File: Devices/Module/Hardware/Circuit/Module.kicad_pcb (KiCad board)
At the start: 2 copper layers, 7 parts, among them J1 Screw_Terminal_01x03, J2 Screw_Terminal_01x04, J3 Screw_Terminal_01x02, Q1 Q_NPN_BCE, Q2 Q_NPN_BCE

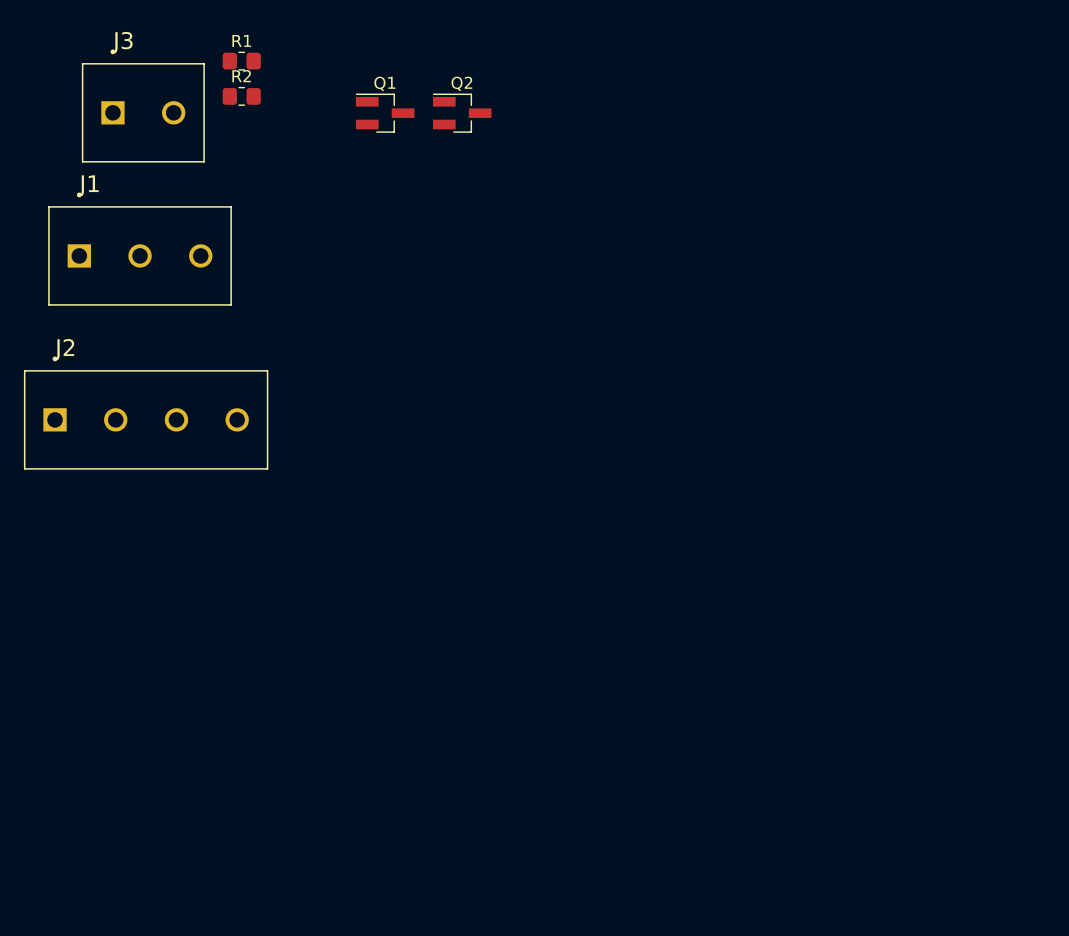
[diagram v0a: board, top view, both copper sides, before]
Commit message: Finish module PCB layout
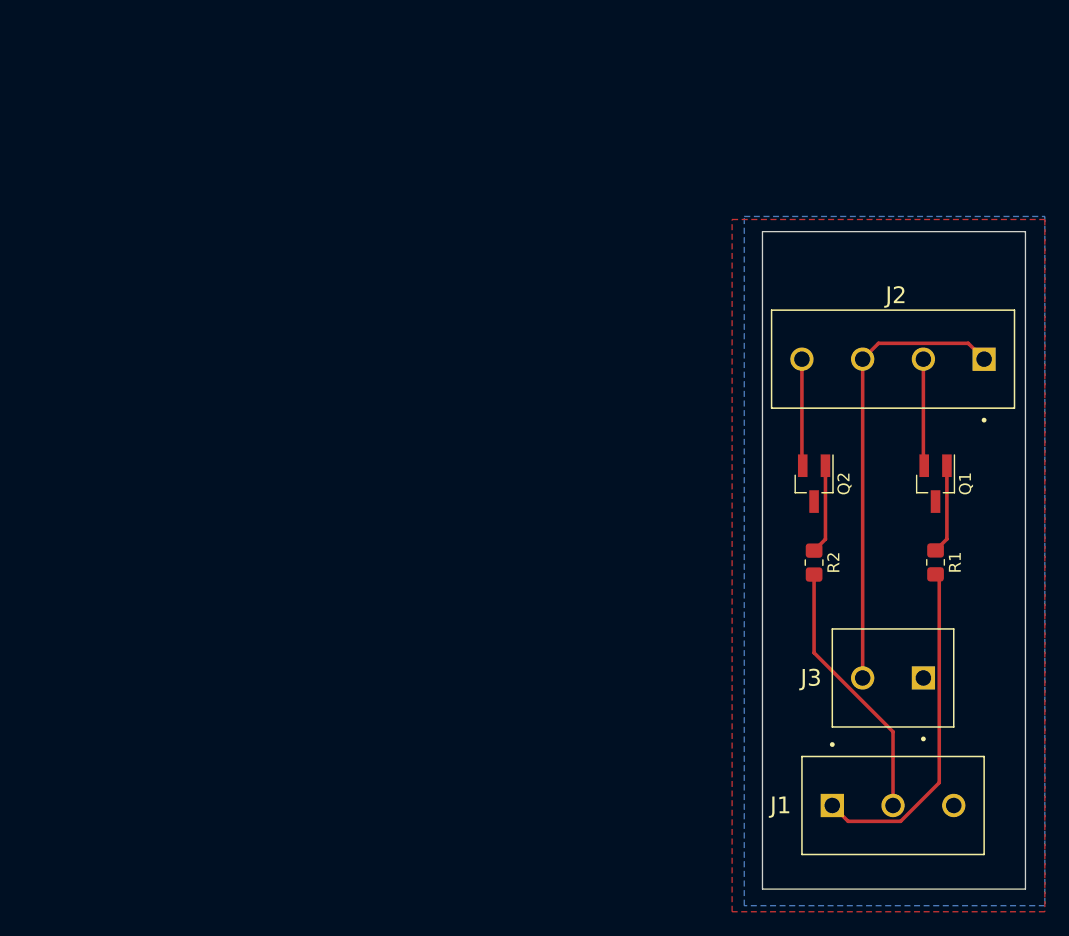
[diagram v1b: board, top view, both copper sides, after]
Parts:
- moved J3 82.7 mm to (150.1, 84.1), turned to 180 degrees
- moved J1 78.0 mm to (142.5, 94.7)
- moved J2 77.9 mm to (155.2, 57.4), turned to 180 degrees
- moved R1 71.6 mm to (151.1, 74.4), turned to 270 degrees
- moved R2 61.8 mm to (141.0, 74.4), turned to 270 degrees
- moved Q1 55.5 mm to (151.1, 67.8), turned to 270 degrees
- moved Q2 42.7 mm to (141.0, 67.8), turned to 270 degrees
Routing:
- net VCC: track 0.00 -> 37.9 mm
- net SIG1: track 0.00 -> 28.4 mm
- net SIG2: track 0.00 -> 22.1 mm
- net LED2N: track 0.00 -> 8.94 mm
- net LED1N: track 0.00 -> 8.94 mm
- net Net-(Q2-Pad1): track 0.00 -> 7.50 mm
- net Net-(Q1-Pad1): track 0.00 -> 7.48 mm
- added copper zone on B.Cu, net GND
- added copper zone on F.Cu, net GND
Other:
- board outline added: 22 x 55 mm
- board text added: "GHOSCHT - 2021"
- board text added: "v01"

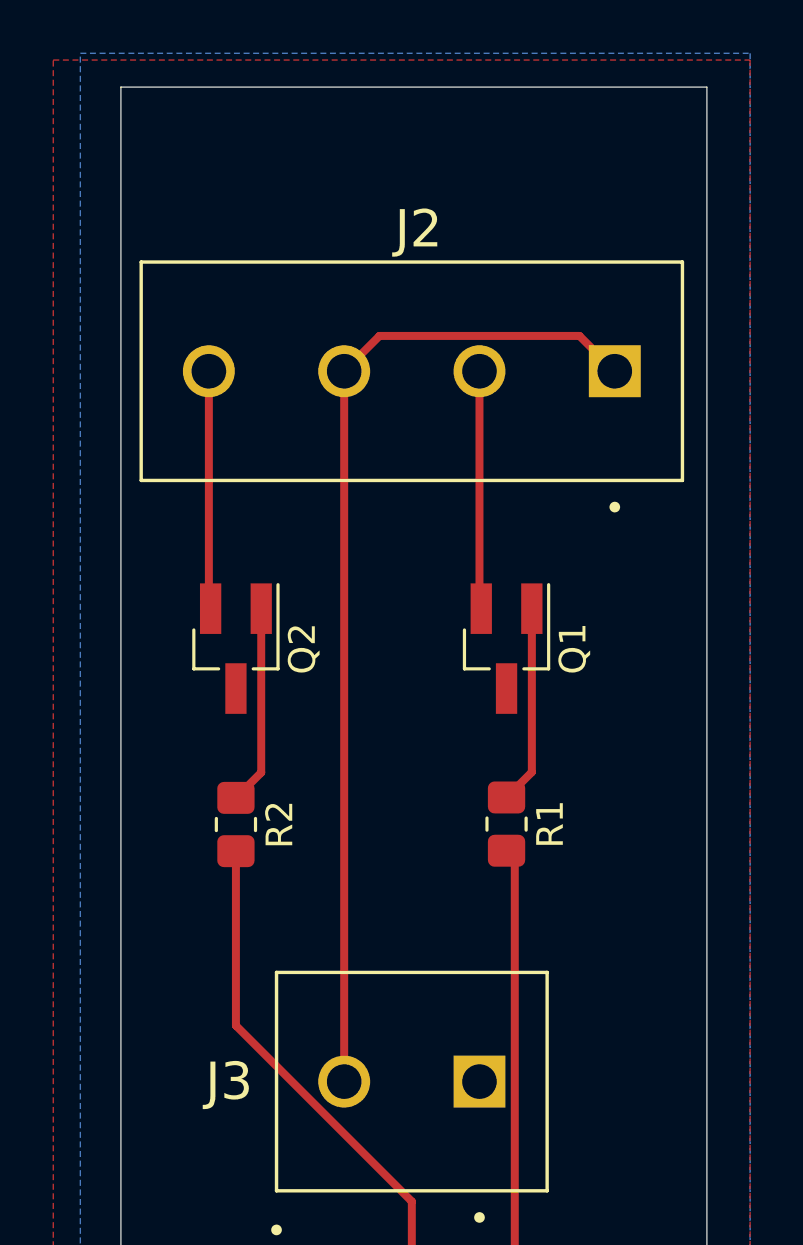
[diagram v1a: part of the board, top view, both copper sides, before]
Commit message: Add pulldown resistor
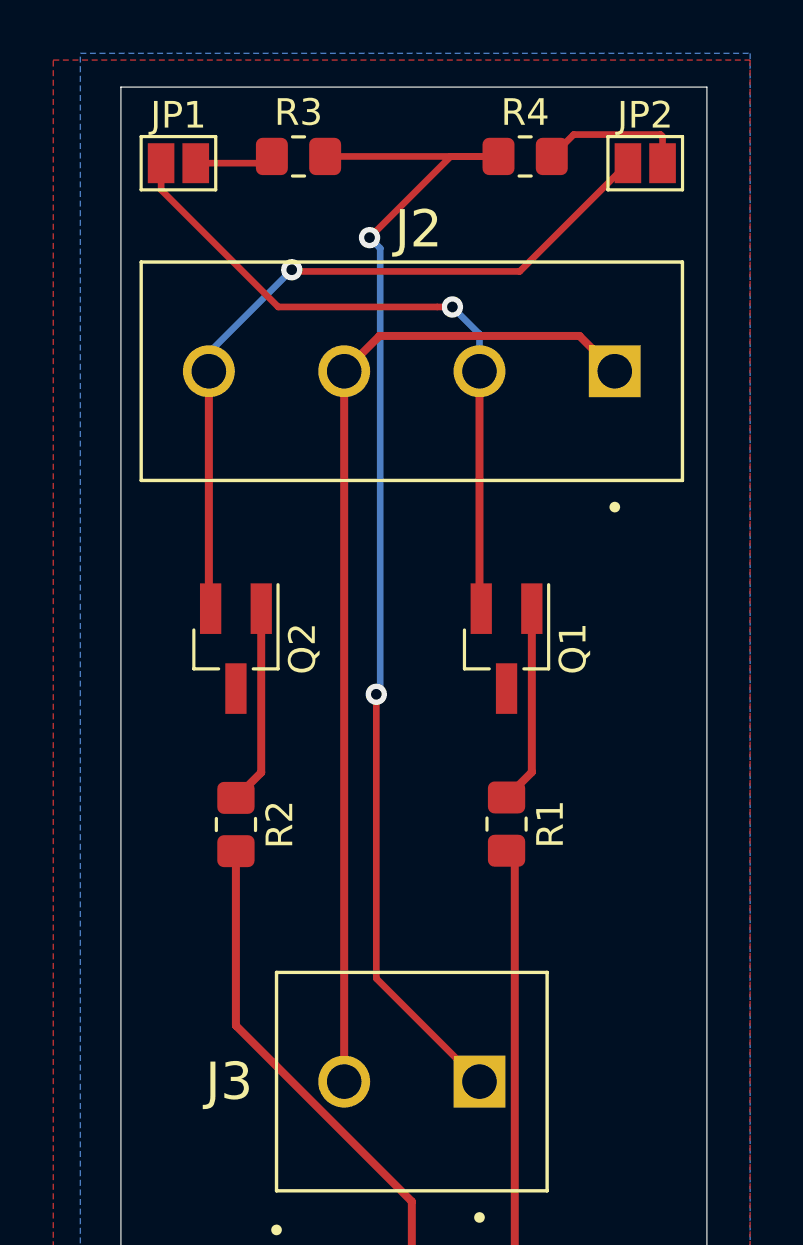
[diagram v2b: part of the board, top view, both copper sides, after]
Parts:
- added JP1: Jumper, Jumper:SolderJumper-2_P1.3mm_Open_Pad1.0x1.5mm, F.Cu at (138.8, 49.6)
- added JP2: Jumper, Jumper:SolderJumper-2_P1.3mm_Open_Pad1.0x1.5mm, F.Cu at (156.3, 49.6)
- added R3: 10k, Resistor_SMD:R_0805_2012Metric_Pad1.20x1.40mm_HandSolder, F.Cu at (143.3, 49.3)
- added R4: 10k, Resistor_SMD:R_0805_2012Metric_Pad1.20x1.40mm_HandSolder, F.Cu at (151.8, 49.3)
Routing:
- net GND: track 0.00 -> 46.1 mm, vias 0 -> 2
- net LED2N: track 8.94 -> 28.4 mm, vias 0 -> 1
- net LED1N: track 8.94 -> 25.5 mm, vias 0 -> 1
- net Net-(JP2-Pad2): track 0.00 -> 5.53 mm
- net Net-(JP1-Pad2): track 0.00 -> 2.96 mm

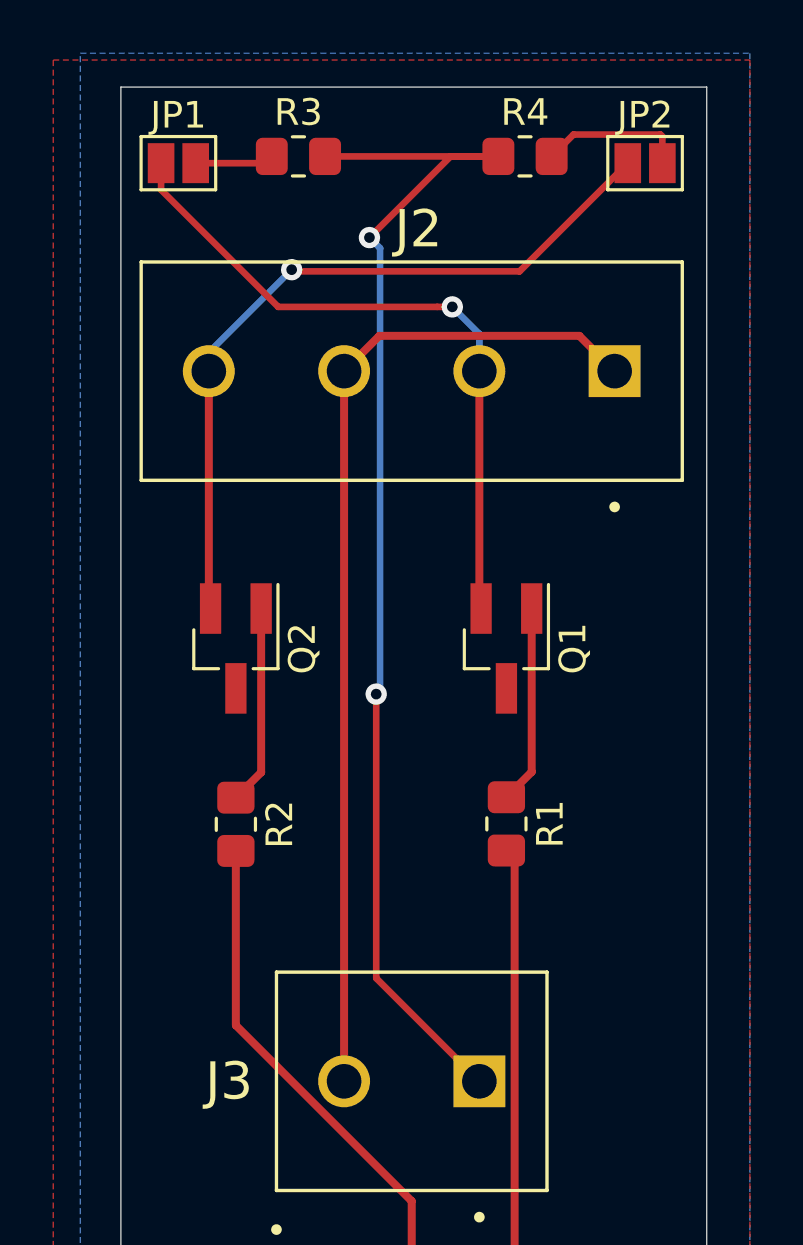
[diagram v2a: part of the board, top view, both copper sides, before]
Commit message: Change pulldown track width
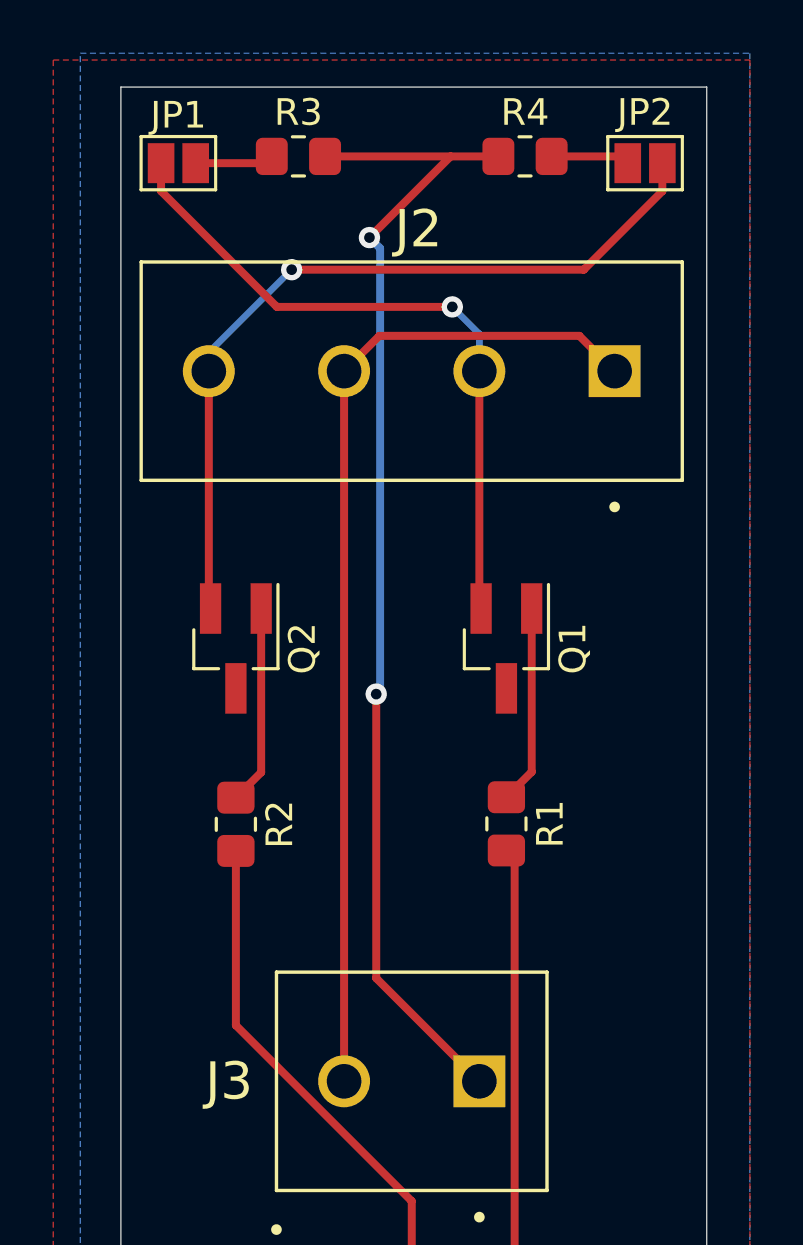
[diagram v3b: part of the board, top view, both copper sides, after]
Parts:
- turned JP2 to 180 degrees
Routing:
- net Net-(JP2-Pad2): track 5.53 -> 3.32 mm
- net LED2N: track 28.4 -> 30.3 mm

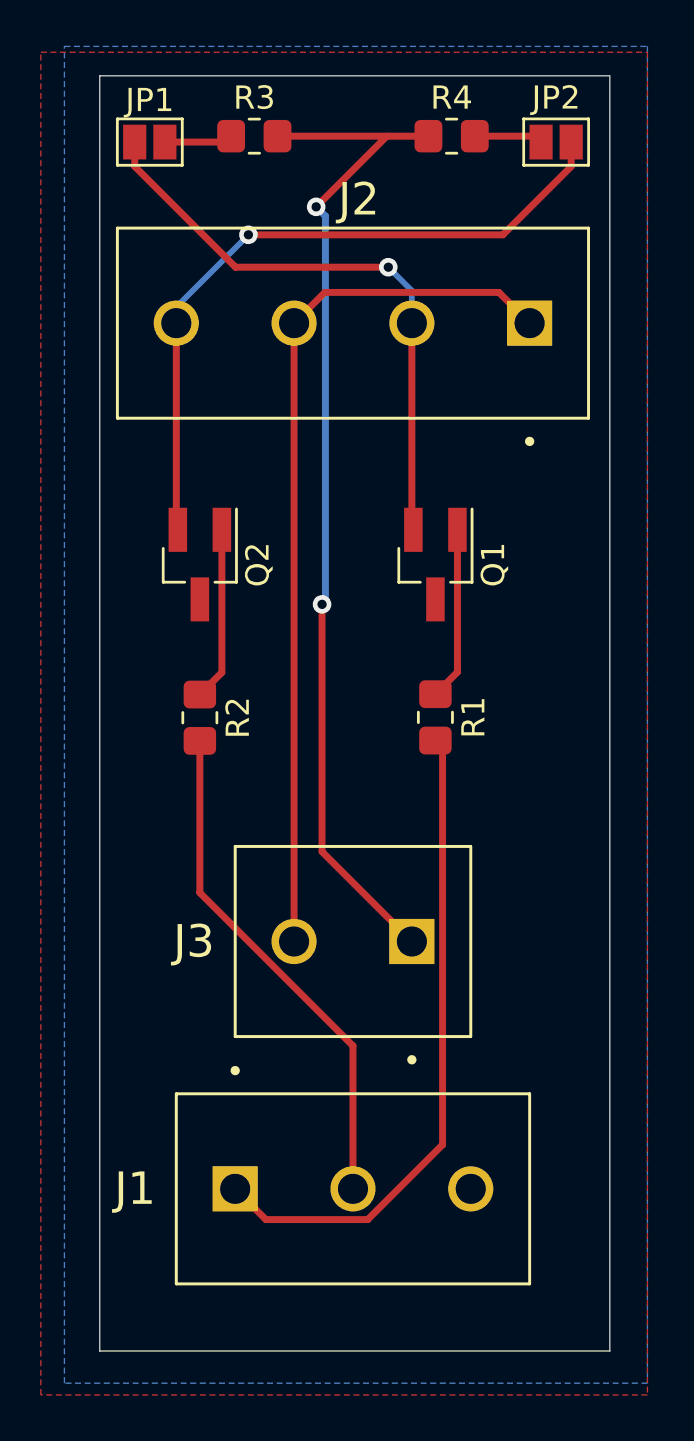
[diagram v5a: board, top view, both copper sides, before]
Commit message: Add port names on silkscreen
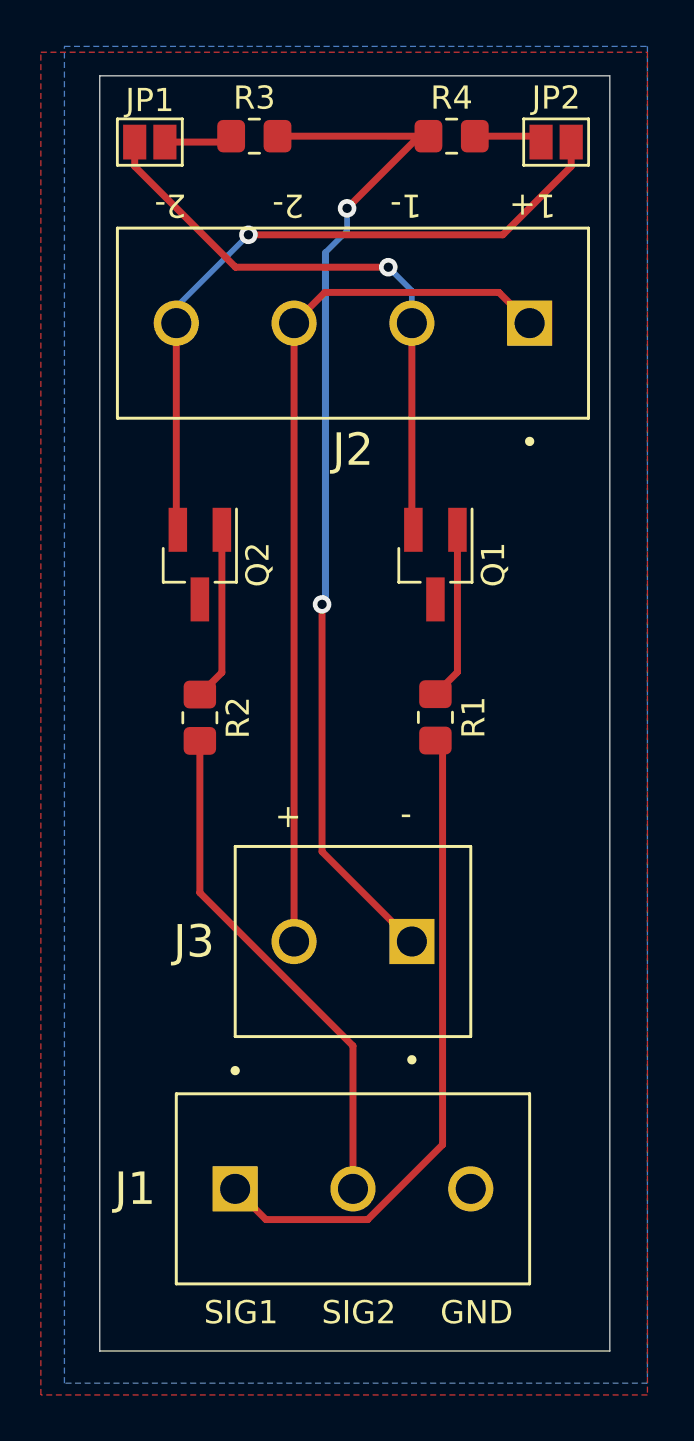
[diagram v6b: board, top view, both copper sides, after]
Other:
- board text added: "+"
- board text added: "-"
- board text added: "1+"
- board text added: "1-"
- board text added: "2-"
- board text added: "20.08.2021"
- board text added: "Designed by: GHOSCHT"
- board text added: "GND"
- board text added: "SIG1"
- board text added: "SIG2"
- board text removed: "GHOSCHT - 2021"
